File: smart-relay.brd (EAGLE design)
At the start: 31 x 55.5 mm, 13 parts, among them U1 RFD22301

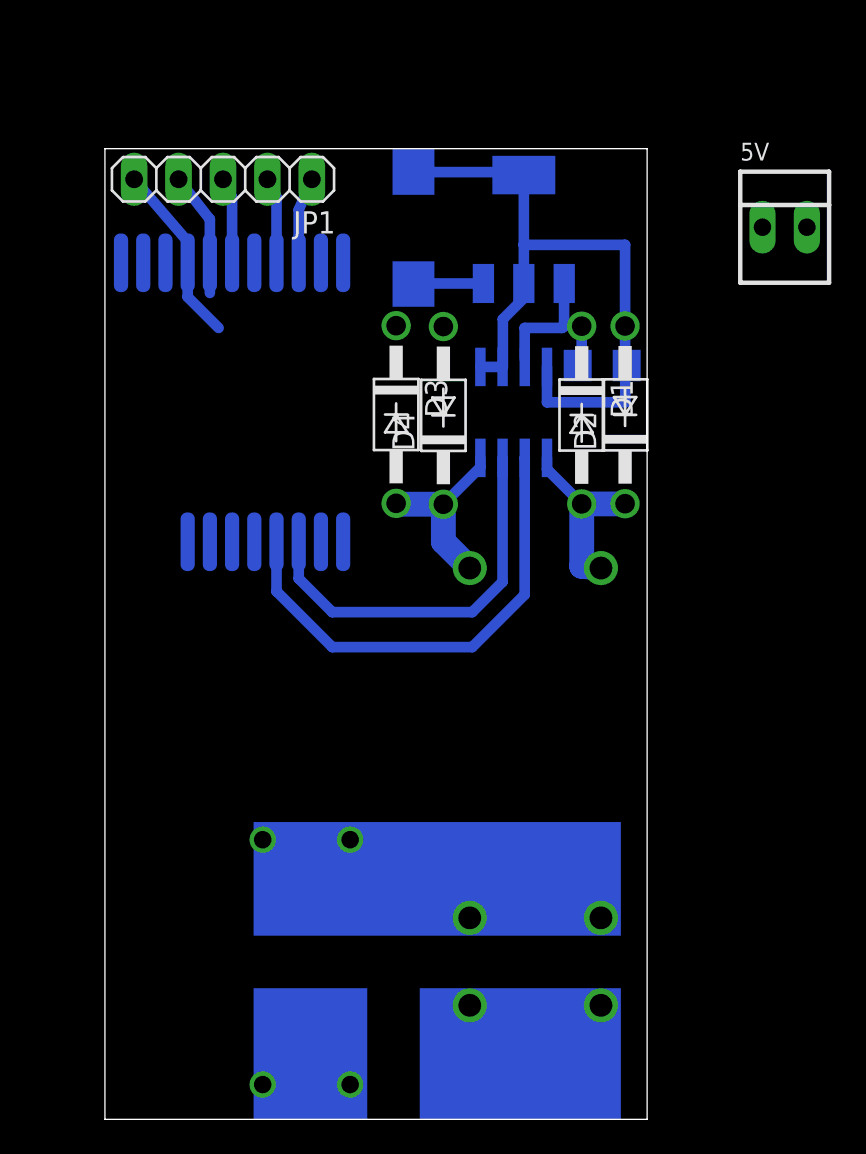
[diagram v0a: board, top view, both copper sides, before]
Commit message: Added LED and moved trace outside of bluetooth.
* Added a bicolor LED in parallel with the relay coil to make debugging
  easier.
* Moved trace from under rfd22301 place so the PCB can be cut and the
  rfd22301 can pe soldered in line with the rest of the PCB. Removing
  the rfd22301 will be easier this way.
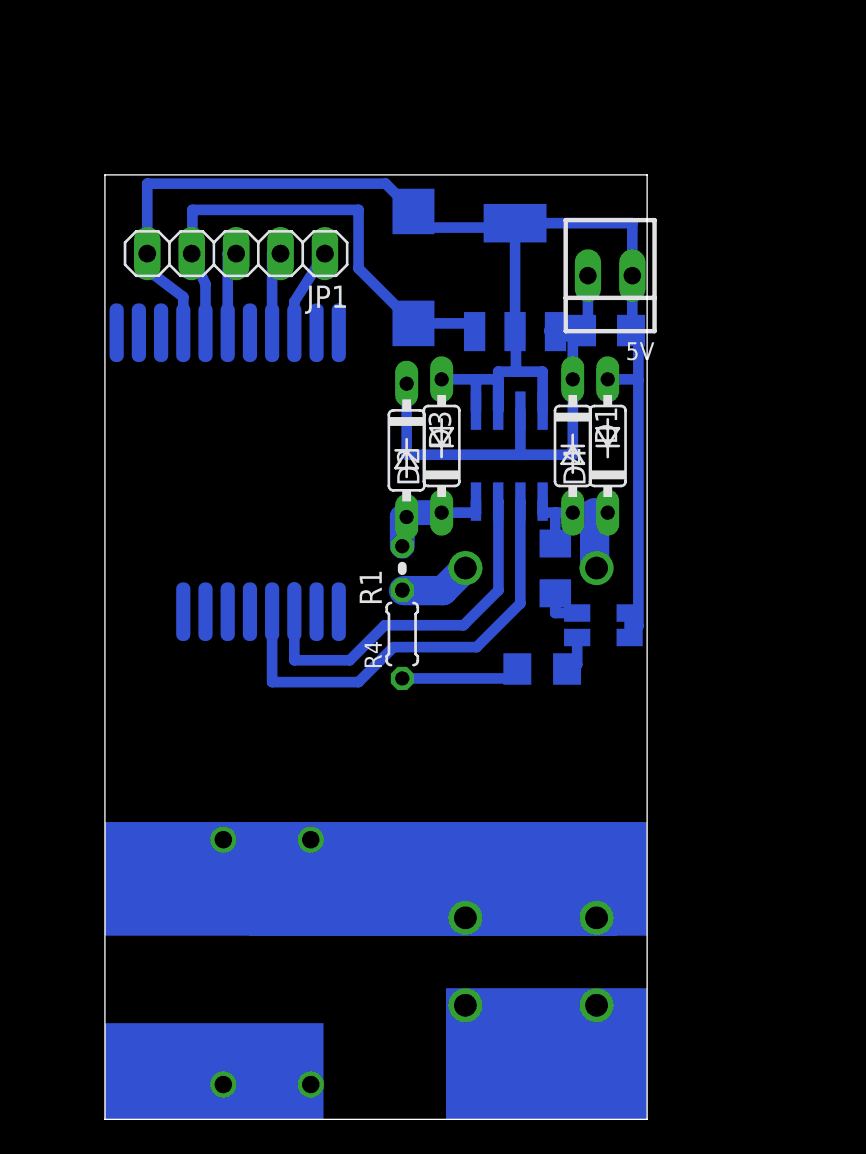
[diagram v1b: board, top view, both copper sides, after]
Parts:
- added D5: OSRG1206C1C, something:OSRG1206C1C
- added R1: (no value), rcl:0204V
- added R2, R3: (no value), eagle-ltspice:R1206
- added R4: (no value), rcl:0204/5
- D1, D2, D3, D4: value 1N4001 -> 1N4148DO35-7; device diode:DO41-10 -> diode:DO35-7
- moved D2 10.6 mm to (19.2, 38.5)
- moved 5V 10.4 mm to (28.9, 48.2), turned to 180 degrees
- moved D4 9.56 mm to (28.8, 38.5)
- moved JP1 4.32 mm to (7.50, 49.5)
- moved U1 4.01 mm to (5.75, 37.0)
- moved LM3904 2.80 mm to (23.4, 48.1)
- moved U$2 2.51 mm to (23.1, 37.9)
- moved C2 2.25 mm to (17.6, 48.7)
- moved FUSE 2.25 mm to (11.8, 1.99)
- moved D3 2.14 mm to (17.2, 38.2)
- moved C1 2.02 mm to (28.7, 45.1)
- moved D1 1.84 mm to (26.8, 38.5)
- moved U$1 0.25 mm to (20.6, 6.52)
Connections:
- new net N$13: R1.1, R4.2, U$1.A1(1)
- new net N$14: R2.2, R4.1
- new net N$15: D5.4, R2.1
- new net N$16: D5.2, R3.1
- net N$10: now also D4.C, R3.2; no longer D2.C
- net N$7: now also D5.1, D5.3
- net N$9: now also D2.C, R1.2; no longer D4.C, U$1.A1(1)
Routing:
- net N$7: track 51.6 -> 88.6 mm
- net N$6: track 10.0 -> 28.8 mm
- net N$8: track 11.1 -> 29.4 mm
- net N$14: track 0.00 -> 7.12 mm
- net N$13: track 0.00 -> 4.14 mm
- net N$9: track 10.6 -> 6.76 mm
- net N$16: track 0.00 -> 2.38 mm
- net N$15: track 0.00 -> 2.18 mm
- net N$1: track 32.5 -> 34.4 mm
- net N$5: track 27.4 -> 26.1 mm
- net N$10: track 10.6 -> 9.40 mm
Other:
- board size 31 x 55.5 mm -> 31 x 54 mm

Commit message: added copper pour 2mm clearance
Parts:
- moved 5V 4.00 mm to (28.9, 52.2)
- moved C1 4.00 mm to (28.7, 49.1)
- moved C2 4.00 mm to (17.6, 52.7)
- moved D1 4.00 mm to (26.8, 42.5)
- moved D2 4.00 mm to (19.2, 42.5)
- moved D3 4.00 mm to (17.2, 42.2)
- moved D4 4.00 mm to (28.8, 42.5)
- moved D5 4.00 mm to (28.5, 32.2)
- moved FUSE 4.00 mm to (11.8, 5.99)
- moved JP1 4.00 mm to (7.50, 53.5)
- moved LM3904 4.00 mm to (23.4, 52.1)
- moved R1 4.00 mm to (17.0, 35.5)
- moved R2 4.00 mm to (25.0, 29.8)
- moved R3 4.00 mm to (25.8, 35.5)
- moved R4 4.00 mm to (17.0, 31.8)
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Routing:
- added copper zone on layer 16, net N$17
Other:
- board outline removed
